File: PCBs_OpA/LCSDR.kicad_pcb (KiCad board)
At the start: 2 copper layers, 70 x 100 mm, 118 parts, among them CON2 AVR-ISP-6, J1 MIC, J10 SPK, J12 Conn_01x01, J13 Conn_01x01, J14 Conn_01x01, J15 Conn_01x01, J2 ANT, J3 USB_B, J4 CAL, J5 MEASURE, J6 I2C, J7 MEASURE, J8 Jack-DC, K1 TIANBO-HJR-4102-L, Q1 2N7002, Q2 2N7002, Q4 BS170, Q6 BS170, Q7 BF998, Q8 BS170, Q9 BC849, U1 74AC14, U2 Si5351, U3 FT232RL, U4 LM1117-5.0, U5 LM1117-3.3, U6 ATMEGA328P-AU, U7 NE5532, Y1 25Mhz, Y2 20Mhz

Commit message: operational amplifier Direct detection receiver
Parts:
- removed C23: 10nF, LCSDR:C_1206_0603
- removed L19: 1uH, Choke_Axial_ThroughHole:Choke_Horizontal_RM10mm
- added C21: 1nF, LCSDR:C_1206_0603, F.Cu at (146.6, 99.8)
- C45: value 330pF -> 360pF
- C47: value 220pF -> 360pF
- C49: value 330pF -> 1nF
- L10, L6, L8: footprint Choke_Axial_ThroughHole:Choke_Horizontal_RM20mm -> Choke_Toroid_ThroughHole:Choke_Toroid_6,5x13mm_Vertical
- L13: footprint Choke_Axial_ThroughHole:Choke_Horizontal_RM10mm -> Choke_Toroid_ThroughHole:Choke_Toroid_6,5x13mm_Vertical
- L15: footprint Resistors_THT:R_Axial_DIN0309_L9.0mm_D3.2mm_P2.54mm_Vertical -> Choke_Toroid_ThroughHole:Choke_Toroid_6,5x13mm_Vertical
- L17: value 680nH -> 1uH; footprint Choke_Axial_ThroughHole:Choke_Horizontal_RM10mm -> Choke_Toroid_ThroughHole:Choke_Toroid_6,5x13mm_Vertical
- moved C36 41.3 mm to (167.6, 66.8), turned to 90 degrees
- moved C9 33.0 mm to (139.2, 90.9), turned to 270 degrees
- moved L5 32.5 mm to (164.6, 121.9), turned to 180 degrees
- moved C34 32.3 mm to (156.2, 66.8)
- moved C27 31.9 mm to (164.8, 99.8), turned to 180 degrees
- moved Q8 30.7 mm to (167.9, 104.4)
- moved Q4 30.5 mm to (167.9, 112.0)
- moved Q6 30.4 mm to (167.9, 119.6)
- moved C25 29.2 mm to (161.0, 108.7), turned to 0 degrees
- moved C8 28.2 mm to (144.3, 95.2)
- moved R14 28.1 mm to (161.8, 122.4)
- moved K1 26.0 mm to (167.1, 84.1)
- moved D2 25.2 mm to (163.3, 91.7)
- moved L15 24.8 mm to (133.3, 108.0), turned to 0 degrees
- moved Q9 24.3 mm to (155.4, 91.9)
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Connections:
- C45 pad 1: RF_IN -> Net-(C21-Pad2)
- L13 pad 1: RF_IN -> Net-(C21-Pad2)
- Q7 pad 4: Net-(C23-Pad1) -> HPF
- R9 pad 1: Net-(C23-Pad1) -> HPF
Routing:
- net +12V: track 147.2 -> 32.5 mm, vias 4 -> 2
- net +5V: track 209.3 -> 108.5 mm, vias 6 -> 4
- net CLK0: track 57.5 -> 0.00 mm, vias 2 -> 0
- net Net-(C25-Pad1): track 49.0 -> 0.00 mm
- net Net-(C27-Pad1): track 43.7 -> 0.00 mm, vias 1 -> 0
- net Net-(C25-Pad2): track 40.2 -> 0.00 mm
- net RX_TX: track 30.1 -> 0.00 mm, vias 2 -> 0
- net Net-(C34-Pad1): track 28.6 -> 0.00 mm
- net LPF: track 27.5 -> 0.00 mm
- net +12VA: track 21.8 -> 0.00 mm
- net RF_IN: track 17.8 -> 0.00 mm, vias 1 -> 0
- net Net-(C30-Pad1): track 26.1 -> 12.0 mm
- net HPF: track 13.5 -> 0.63 mm, vias 1 -> 0
- net Net-(C32-Pad1): track 14.8 -> 2.80 mm
- net Net-(C45-Pad2): track 10.9 -> 0.00 mm
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
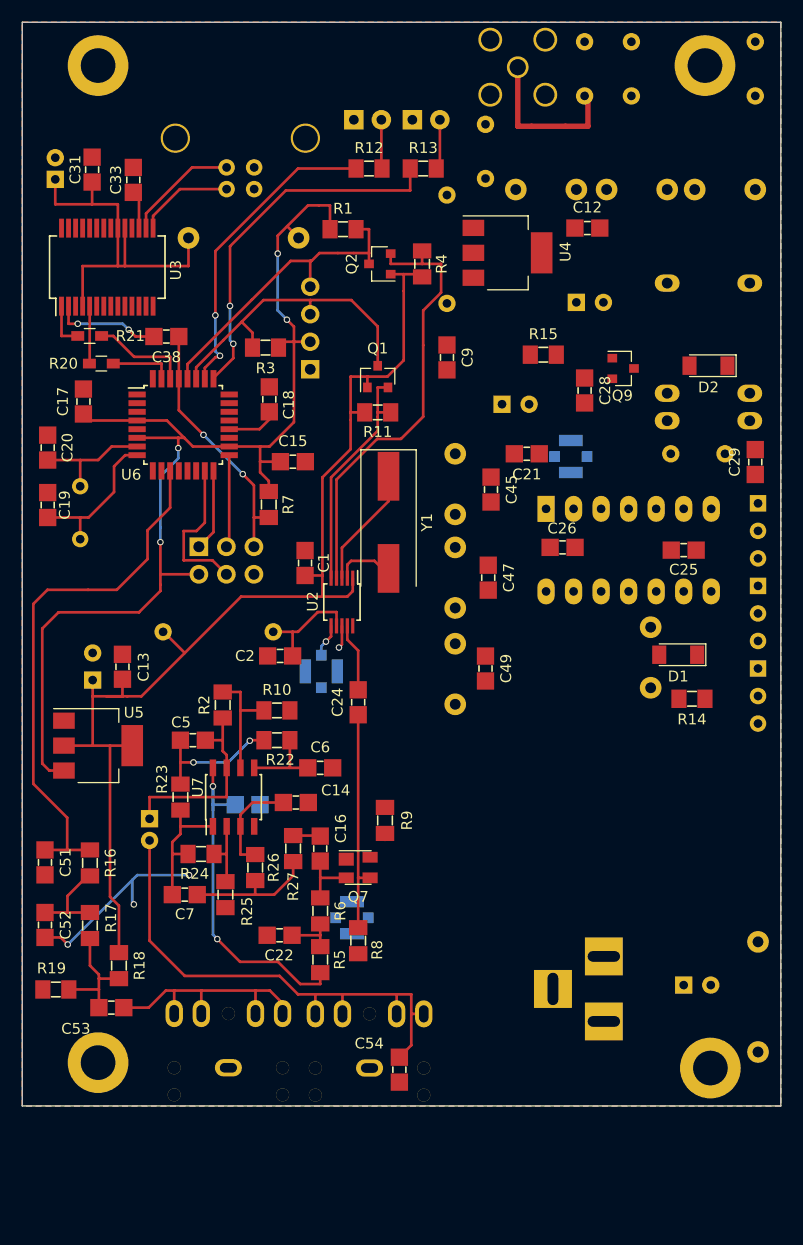
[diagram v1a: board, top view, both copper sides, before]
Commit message: add LPF/HPF RFSimm models
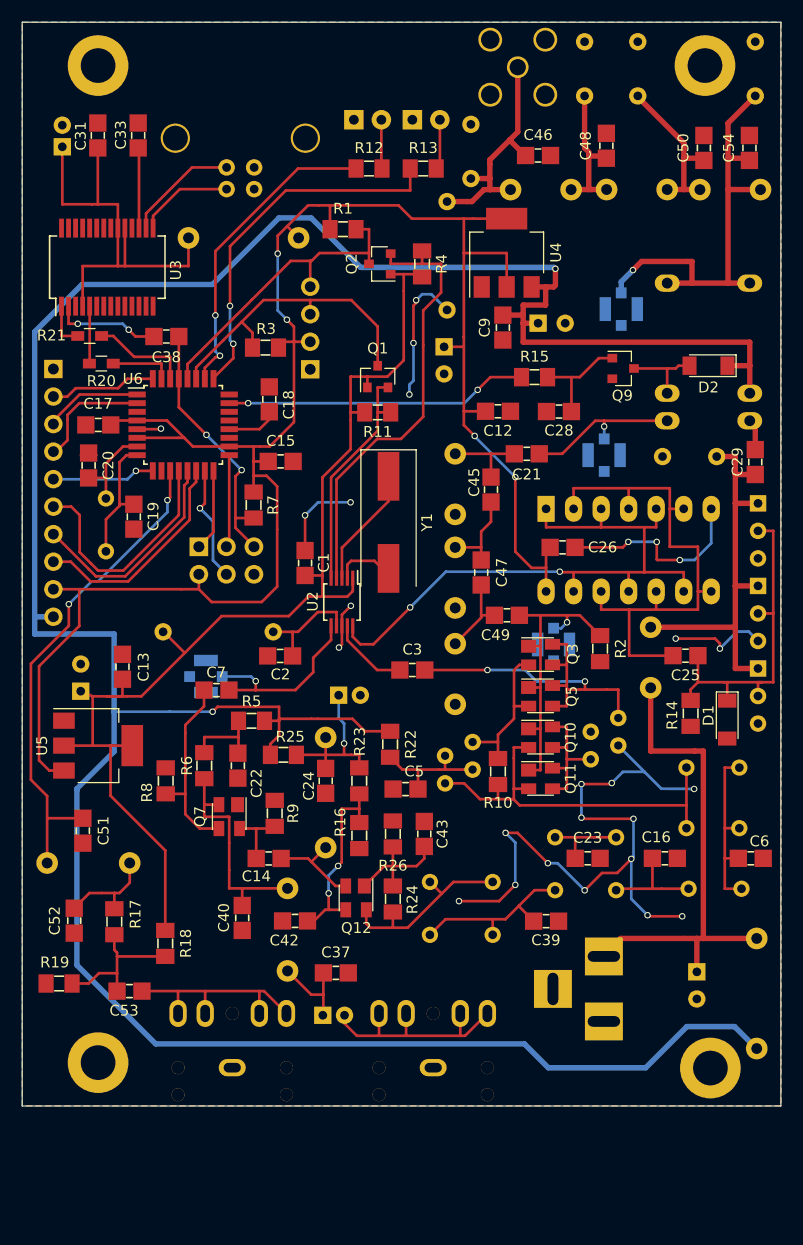
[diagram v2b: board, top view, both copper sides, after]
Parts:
- removed R27: 910, LCSDR:R_1206_0603
- removed U7: NE5532, Housings_SOIC:SOIC-8_3.9x4.9mm_Pitch1.27mm
- added C23: 56pF, LCSDR:C_1206_0603, F.Cu at (152.2, 137.2)
- added C37: 100nF, LCSDR:C_1206_0603, F.Cu at (128.9, 147.7)
- added C39: 56pF, LCSDR:C_1206_0603, F.Cu at (148.3, 142.9)
- added C40: 100nF, LCSDR:C_1206_0603, F.Cu at (120.3, 142.7)
- added C41: 10uF, Capacitors_THT:CP_Radial_D5.0mm_P2.00mm, B.Cu at (129.2, 122.1)
- added C42: 100nF, LCSDR:C_1206_0603, F.Cu at (125.2, 142.9)
- added C43: 100nF, LCSDR:C_1206_0603, F.Cu at (137.1, 134.9)
- added C46: 360pF, LCSDR:C_1206_0603, F.Cu at (147.6, 72.3)
- added C48: 750pF, LCSDR:C_1206_0603, F.Cu at (153.9, 71.4)
- added C50: 750pF, LCSDR:C_1206_0603, F.Cu at (162.9, 71.6)
- added J11: Conn_01x10, Pin_Headers:Pin_Header_Straight_1x10_Pitch2.54mm, B.Cu at (102.9, 92.0)
- added J9: MEASURE, LCSDR:U.FL_Molex_MCRF_73412-0110_Vertical, B.Cu at (155.3, 86.5)
- added L3: 100uH, Choke_Axial_ThroughHole:Choke_Horizontal_RM10mm, B.Cu at (128.0, 131.0)
- added L4: 100mH, Choke_Toroid_ThroughHole:Choke_Toroid_8x16mm_Vertical, B.Cu at (132.1, 147.5)
- added L7: 100mH, Choke_Toroid_ThroughHole:Choke_Toroid_8x16mm_Vertical, B.Cu at (102.3, 145.2)
- added Q10: BF998, TO_SOT_Packages_SMD:SOT-143, F.Cu at (147.8, 126.0)
- added Q11: BF998, TO_SOT_Packages_SMD:SOT-143, F.Cu at (147.8, 129.8)
- added Q12: BF998, TO_SOT_Packages_SMD:SOT-143, F.Cu at (130.8, 140.8)
- added Q3: BF998, TO_SOT_Packages_SMD:SOT-143, F.Cu at (147.8, 118.3)
- added Q5: BF998, TO_SOT_Packages_SMD:SOT-143, F.Cu at (147.8, 122.2)
- added T1: Transformer_1_4, LCSDR:TF14, B.Cu at (155.0, 124.2)
- added T2: Transformer_1_4, LCSDR:TF14, B.Cu at (141.6, 126.4)
- added Y3: Crystal, Crystals:Crystal_HC49-U_Vertical, B.Cu at (161.3, 134.4)
- added Y4: Crystal, Crystals:Crystal_HC49-U_Vertical, B.Cu at (161.3, 128.8)
- added Y5: Crystal, Crystals:Crystal_HC49-U_Vertical, B.Cu at (166.4, 140.0)
- added Y6: Crystal, Crystals:Crystal_HC49-U_Vertical, B.Cu at (154.8, 140.1)
- added Y7: Crystal, Crystals:Crystal_HC49-U_Vertical, B.Cu at (149.2, 135.2)
- added Y8: Crystal, Crystals:Crystal_HC49-U_Vertical, B.Cu at (137.6, 144.2)
- added Y9: Crystal, Crystals:Crystal_HC49-U_Vertical, B.Cu at (143.4, 144.2)
- C14, C7: value 27nF -> 10nF
- C16: value 1uF -> 56pF
- C24, C51, C52: value 10nF -> 100nF
- C3: value 100nF -> 10nF; moved to F.Cu
- C30, C36: value 270pF -> 360pF
- C32, C34: value 680pF -> 750pF
- C5: value 33nF -> 100nF
- C53: value 100nF -> 1uF
- C54: value 100nF -> 360pF
- C6: value 33nF -> 56pF
- L10, L6: value 1.32uH -> 1.22uH
- L8: value 1.72uH -> 1.42uH
- R10: value 910 -> 1.5K
- R16: value 10k -> 10K
- R2: value 2K -> 220
- R22: value 2.7K -> 100
- R23: value 1.2K -> 10K
- R24: value 2K -> 300
- R25: value 910 -> 100
- R26: value 5.1K -> 220
- moved C54 91.0 mm to (167.1, 71.6), turned to 90 degrees
- moved C6 40.6 mm to (167.2, 137.2)
- moved R2 35.2 mm to (153.3, 117.8)
- moved C16 31.8 mm to (159.3, 137.2), turned to 0 degrees
- moved J7 31.3 mm to (149.0, 117.4), turned to 0 degrees
- moved R16 25.0 mm to (131.1, 135.1)
- moved C4 24.2 mm to (127.7, 151.6), turned to 0 degrees
- moved R8 23.1 mm to (113.2, 130.0), turned to 90 degrees
- moved R5 22.9 mm to (121.2, 124.5), turned to 0 degrees
- moved R10 21.2 mm to (143.9, 129.1), turned to 90 degrees
- moved C5 20.1 mm to (135.4, 130.8), turned to 0 degrees
- moved C3 19.6 mm to (136.0, 119.8)
- moved C7 19.1 mm to (117.9, 121.6)
- moved C12 18.8 mm to (143.9, 95.9)
- moved R24 18.2 mm to (134.2, 140.9), turned to 90 degrees
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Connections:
- C14 pad 2: GND -> Net-(C14-Pad2)
- C16 pad 2: Net-(C16-Pad2) -> GND
- C24 pad 2: CLK1 -> GND
- C3 pad 1: +12V -> CLK1
- C3 pad 2: GND -> Net-(C3-Pad2)
- C4 pad 1: Net-(C4-Pad1) -> Net-(C37-Pad1)
- C5 pad 1: Net-(C4-Pad1) -> GND
- C51 pad 1: Net-(C51-Pad1) -> MIC
- C54 pad 1: Net-(C4-Pad2) -> LPF
- C7 pad 2: Net-(C7-Pad2) -> CLK2
- J4 pad 1: Net-(J4-Pad1) -> CLK2
- Q7 pad 2: Net-(C16-Pad2) -> Net-(C40-Pad1)
- Q7 pad 3: Net-(C24-Pad1) -> Net-(C7-Pad1)
- Q7 pad 4: HPF -> Net-(C14-Pad2)
- R10 pad 1: Net-(R10-Pad1) -> Net-(Q10-Pad2)
- R10 pad 2: GND -> Net-(Q3-Pad2)
- R16 pad 1: Net-(C51-Pad1) -> Net-(C42-Pad1)
- R16 pad 2: Net-(C52-Pad1) -> GND
- R2 pad 1: Net-(R10-Pad1) -> HPF
- R2 pad 2: Net-(C4-Pad1) -> GND
- R22 pad 1: Net-(C5-Pad2) -> +12V
- R22 pad 2: Net-(C6-Pad1) -> Net-(C5-Pad2)
- R23 pad 1: Net-(C7-Pad1) -> Net-(C24-Pad1)
- R23 pad 2: Net-(C5-Pad2) -> Net-(C42-Pad1)
- R24 pad 1: Net-(R24-Pad1) -> Net-(Q12-Pad4)
- R24 pad 2: Net-(C7-Pad1) -> Net-(C43-Pad1)
- R25 pad 1: Net-(R24-Pad1) -> +12V
- R25 pad 2: GND -> Net-(C24-Pad1)
- R26 pad 1: Net-(C7-Pad2) -> Net-(C43-Pad1)
- R26 pad 2: Net-(C14-Pad1) -> GND
- R6 pad 1: Net-(C16-Pad2) -> Net-(C40-Pad1)
- R8 pad 1: Net-(C24-Pad1) -> Net-(C7-Pad1)
- R9 pad 1: HPF -> Net-(C14-Pad2)
- U2 pad 6: Net-(J4-Pad1) -> CLK2
- U6 pad 1: (no net) -> IO_5
- U6 pad 11: Net-(C51-Pad1) -> MIC
- U6 pad 12: (no net) -> IO_8
- U6 pad 13: (no net) -> IO_9
- U6 pad 14: RX_TX -> IO_10
- U6 pad 2: (no net) -> IO_6
- U6 pad 23: (no net) -> RX_TX
- U6 pad 32: (no net) -> IO_4
- U6 pad 9: (no net) -> IO_7
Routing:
- net +12V: track 32.5 -> 267.5 mm
- net GND: track 20.6 -> 117.9 mm, vias 4 -> 26
- net +5V: track 108.5 -> 182.7 mm
- net CLK0: track 0.00 -> 59.3 mm, vias 0 -> 2
- net Net-(C25-Pad1): track 0.00 -> 49.6 mm
- net Net-(C51-Pad1): track 49.4 -> 0.00 mm
- net +12VA: track 0.00 -> 45.9 mm
- net MIC: track 0.00 -> 45.8 mm, vias 0 -> 2
- net LPF: track 0.00 -> 41.2 mm, vias 0 -> 1
- net Net-(Q10-Pad2): track 0.00 -> 37.6 mm
- net Net-(C27-Pad1): track 0.00 -> 37.2 mm
- net Net-(C3-Pad2): track 0.00 -> 34.3 mm, vias 0 -> 2
- net Net-(C25-Pad2): track 0.00 -> 31.5 mm
- net HPF: track 0.63 -> 29.1 mm, vias 0 -> 1
- net RX_TX: track 0.00 -> 28.0 mm, vias 0 -> 2
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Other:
- net class Default: trace_width 0.25 -> 0.5

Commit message: release gerber files
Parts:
- added J17: QER, Pin_Headers:Pin_Header_Straight_1x01_Pitch2.54mm, B.Cu at (142.2, 134.0)
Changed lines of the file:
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@@
 (kicad_pcb (version 4) (host pcbnew 4.0.7)
   (general
-    (links 326)
+    (links 327)
     (no_connects 0)
     (area 99.949999 59.949999 170.050001 160.050001)
@@
     (tracks 904)
     (zones 0)
-    (modules 144)
+    (modules 145)
     (nets 83)
   )
@@
     )
   )
+  (module Pin_Headers:Pin_Header_Straight_1x01_Pitch2.54mm (layer B.Cu)
+    (at 142.25 134)
+    (descr "Through hole straight pin header, 1x01, 2.54mm pitch, single row")
+    (tags "Through hole pin header THT 1x01 2.54mm single row")
+    (fp_text reference J17 (at -2.5 0.25 270) (layer B.SilkS)
+      (effects (font (size 1 1) (thickness 0.15)) (justify mirror))
+    )
+    (fp_text value QER (at 0 -2.33) (layer B.Fab)
+      (effects (font (size 1 1) (thickness 0.15)) (justify mirror))
+    )
+    (fp_line (start -0.635 1.27) (end 1.27 1.27) (layer B.Fab) (width 0.1))
+    (fp_line (start 1.27 1.27) (end 1.27 -1.27) (layer B.Fab) (width 0.1))
+    (fp_line (start 1.27 -1.27) (end -1.27 -1.27) (layer B.Fab) (width 0.1))
+    (fp_line (start -1.27 -1.27) (end -1.27 0.635) (layer B.Fab) (width 0.1))
+    (fp_line (start -1.27 0.635) (end -0.635 1.27) (layer B.Fab) (width 0.1))
+    (fp_line (start -1.33 -1.33) (end 1.33 -1.33) (layer B.SilkS) (width 0.12))
+    (fp_line (start -1.33 -1.27) (end -1.33 -1.33) (layer B.SilkS) (width 0.12))
+    (fp_line (start 1.33 -1.27) (end 1.33 -1.33) (layer B.SilkS) (width 0.12))
+    (fp_line (start -1.33 -1.27) (end 1.33 -1.27) (layer B.SilkS) (width 0.12))
+    (fp_line (start -1.33 0) (end -1.33 1.33) (layer B.SilkS) (width 0.12))
+    (fp_line (start -1.33 1.33) (end 0 1.33) (layer B.SilkS) (width 0.12))
+    (fp_line (start -1.8 1.8) (end -1.8 -1.8) (layer B.CrtYd) (width 0.05))
+    (fp_line (start -1.8 -1.8) (end 1.8 -1.8) (layer B.CrtYd) (width 0.05))
+    (fp_line (start 1.8 -1.8) (end 1.8 1.8) (layer B.CrtYd) (width 0.05))
+    (fp_line (start 1.8 1.8) (end -1.8 1.8) (layer B.CrtYd) (width 0.05))
+    (fp_text user %R (at 0 0 270) (layer B.Fab)
+      (effects (font (size 1 1) (thickness 0.15)) (justify mirror))
+    )
+    (pad 1 thru_hole rect (at 0 0) (size 1.7 1.7) (drill 1) (layers *.Cu *.Mask)
+      (net 1 GND))
+    (model ${KISYS3DMOD}/Pin_Headers.3dshapes/Pin_Header_Straight_1x01_Pitch2.54mm.wrl
+      (at (xyz 0 0 0))
+      (scale (xyz 1 1 1))
+      (rotate (xyz 0 0 0))
+    )
+  )
   (gr_line (start 170 60) (end 170 160) (angle 90) (layer Edge.Cuts) (width 0.1))
   (gr_line (start 100 60) (end 170 60) (angle 90) (layer Edge.Cuts) (width 0.1))
@@
   (segment (start 152.27506 75.439064) (end 152.525 75.438) (width 0.5) (layer F.Cu) (net 31) (status 10))
   (segment (start 152.525 75.438) (end 153.924 75.438) (width 0.5) (layer F.Cu) (net 31))
-  (segment (start 156.8 66.8) (end 156.8 66.9) (width 0.5) (layer F.Cu) (net 32) (status C00000))
-  (segment (start 156.8 66.9) (end 161.05 71.15) (width 0.5) (layer F.Cu) (net 32) (status 400000))
+  (segment (start 156.8 66.8) (end 156.8 66.9) (width 0.5) (layer F.Cu) (net 32))
+  (segment (start 156.8 66.9) (end 161.05 71.15) (width 0.5) (layer F.Cu) (net 32))
   (segment (start 161.05 71.15) (end 161.05 71.642) (width 0.5) (layer F.Cu) (net 32))
   (segment (start 162.9 72.55) (end 161.05 72.55) (width 0.5) (layer F.Cu) (net 32) (status 10))

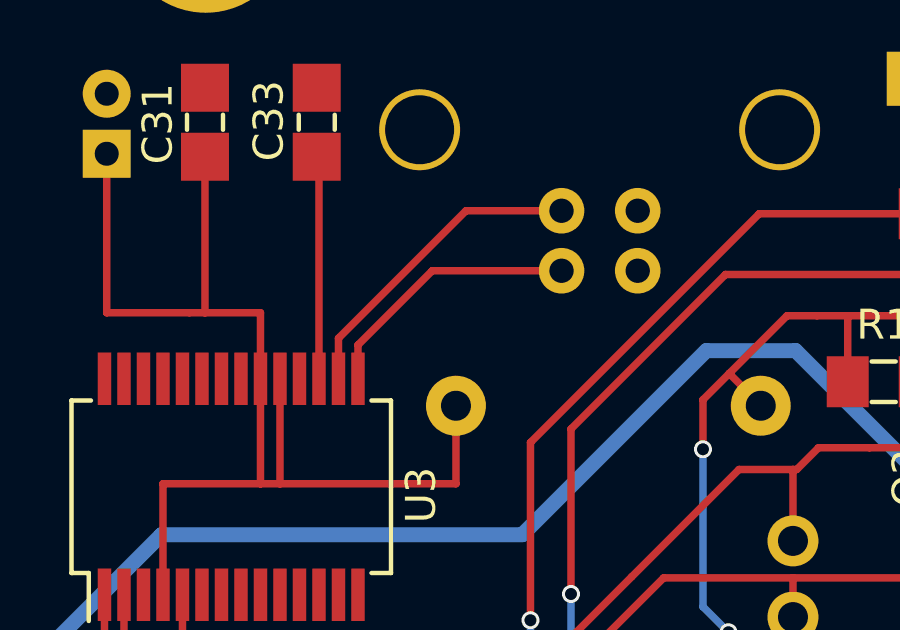
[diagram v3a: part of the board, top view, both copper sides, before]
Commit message: ADX988 CAT: add FE, FI commands
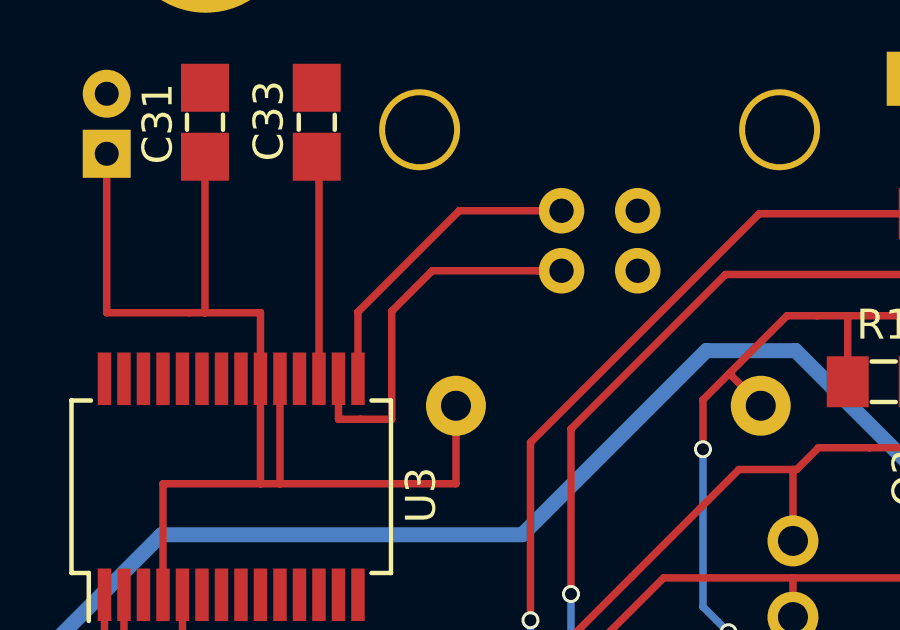
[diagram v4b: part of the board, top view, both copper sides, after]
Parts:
- C21, C49: value 1nF -> 680pF
- C45, C47: value 360pF -> 270pF
- L13, L17: value 1uH -> 900nH
- L15: value 680nH -> 800nH
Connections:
- J3 pad 1: (no net) -> Net-(J3-Pad1)
- U3 pad 10: (no net) -> Net-(U3-Pad10)
- U3 pad 11: (no net) -> Net-(U3-Pad11)
- U3 pad 12: (no net) -> Net-(U3-Pad12)
- U3 pad 13: (no net) -> Net-(U3-Pad13)
- U3 pad 14: (no net) -> Net-(U3-Pad14)
- U3 pad 15: Net-(J3-Pad2) -> Net-(J3-Pad3)
- U3 pad 16: Net-(J3-Pad3) -> Net-(J3-Pad2)
- U3 pad 22: (no net) -> Net-(U3-Pad22)
- U3 pad 23: (no net) -> Net-(U3-Pad23)
- U3 pad 27: (no net) -> Net-(U3-Pad27)
- U3 pad 28: (no net) -> Net-(U3-Pad28)
- U3 pad 3: (no net) -> Net-(U3-Pad3)
- U3 pad 6: (no net) -> Net-(U3-Pad6)
- U3 pad 9: (no net) -> Net-(U3-Pad9)
- U6 pad 19: (no net) -> Net-(U6-Pad19)
- U6 pad 22: (no net) -> Net-(U6-Pad22)
- U6 pad 24: (no net) -> IO_1
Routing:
- net Net-(J3-Pad2): track 8.94 -> 12.9 mm
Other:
- net class Default: trace_width 0.5 -> 0.25

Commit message: Arduino Nano PCB ADX988 DSP
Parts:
- removed C17, C18, C31, C33: 100nF, LCSDR:C_1206_0603
- removed C44: 10uF, Capacitors_THT:CP_Radial_D5.0mm_P2.00mm
- removed D3: LED, LEDs:LED_D3.0mm_Horizontal_O3.81mm_Z10.0mm
- removed J11: Conn_01x10, Pin_Headers:Pin_Header_Straight_1x10_Pitch2.54mm
- removed L12: 10uH, Choke_Axial_ThroughHole:Choke_Horizontal_RM10mm
- removed Q1, Q2: 2N7002, TO_SOT_Packages_SMD:SOT-23
- removed R1, R3: 10K, LCSDR:R_1206_0603
- removed R12: 1k, LCSDR:R_1206_0603
- removed U6: ATMEGA328P-AU, Housings_QFP:TQFP-32_7x7mm_Pitch0.8mm
- added Q13: MMBT3904, TO_SOT_Packages_SMD:SOT-23, F.Cu at (123.0, 81.2)
- added Q14: MMBT3906, TO_SOT_Packages_SMD:SOT-23, F.Cu at (111.3, 78.9)
- added R27: 10K, Resistors_SMD:R_0603_HandSoldering, F.Cu at (119.8, 80.2)
- added R28: 4.7k, Resistors_SMD:R_0603_HandSoldering, F.Cu at (118.3, 71.0)
- J3: value USB_B -> RJ45; footprint Connectors:USB_B -> Connectors:RJ45_8
- R20: value 1K -> 4.7k
- U3: value FT232RL -> ATtiny1614-SS; footprint Housings_SSOP:SSOP-28_5.3x10.2mm_Pitch0.65mm -> Housings_SOIC:SOIC-14_3.9x8.7mm_Pitch1.27mm
- moved C15 70.4 mm to (135.0, 170.1)
- moved C38 20.2 mm to (127.0, 74.2)
- moved R20 14.4 mm to (116.3, 80.2), turned to 0 degrees
- moved U3 11.4 mm to (116.2, 90.3), turned to 0 degrees
- moved R21 8.73 mm to (111.5, 82.0)
- moved J3 6.75 mm to (114.8, 74.2), turned to 0 degrees
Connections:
- C15 pad 1: +5V -> +3V3
- CON2 pad 1: Net-(CON2-Pad1) -> (no net)
- CON2 pad 3: Net-(CON2-Pad3) -> (no net)
- CON2 pad 4: Net-(CON2-Pad4) -> (no net)
- CON2 pad 5: RESET -> (no net)
- J3 pad 1: Net-(J3-Pad1) -> (no net)
- J3 pad 2: Net-(J3-Pad2) -> (no net)
- J3 pad 4: GND -> (no net)
- J6 pad 2: +5V -> +3V3
- R11 pad 2: Net-(Q1-Pad2) -> SDA
- R20 pad 1: TxD -> +3V3
- R20 pad 2: Net-(R20-Pad2) -> TxD
- R21 pad 2: Net-(R21-Pad2) -> Net-(Q14-Pad1)
- R4 pad 2: Net-(Q2-Pad2) -> SCL
- R7 pad 2: RESET -> (no net)
- U2 pad 4: Net-(Q2-Pad2) -> SCL
- U2 pad 5: Net-(Q1-Pad2) -> SDA
- U3 pad 1: Net-(R21-Pad2) -> +3V3
- U3 pad 10: Net-(U3-Pad10) -> RESET
- U3 pad 11: Net-(U3-Pad11) -> RxD
- U3 pad 12: Net-(U3-Pad12) -> TxD
- U3 pad 13: Net-(U3-Pad13) -> (no net)
- U3 pad 14: Net-(U3-Pad14) -> GND
- U3 pad 2: Net-(C38-Pad2) -> LED_RED
- U3 pad 3: Net-(U3-Pad3) -> RX_TX
- U3 pad 4: Net-(C31-Pad1) -> MIC
- U3 pad 5: Net-(R20-Pad2) -> GND
- U3 pad 6: Net-(U3-Pad6) -> Net-(C20-Pad1)
- U3 pad 7: GND -> Net-(C19-Pad1)
- U3 pad 8: (no net) -> SDA
- U3 pad 9: Net-(U3-Pad9) -> SCL
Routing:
- net +12V: track 267.5 -> 184.4 mm, vias 2 -> 1
- net +5V: track 182.7 -> 114.3 mm, vias 4 -> 2
- net Net-(Q2-Pad2): track 41.1 -> 0.00 mm
- net Net-(C31-Pad1): track 40.9 -> 0.00 mm
- net MIC: track 45.8 -> 7.43 mm, vias 2 -> 0
- net +3V3: track 108.1 -> 72.9 mm
- net LED_RED: track 33.9 -> 0.00 mm, vias 2 -> 0
- net (no net): track 0.00 -> 31.9 mm, vias 0 -> 1
- net SDA: track 29.1 -> 0.00 mm
- net LED_GREEN: track 28.8 -> 0.00 mm, vias 2 -> 0
- net RX_TX: track 28.0 -> 0.00 mm, vias 2 -> 0
- net RESET: track 24.4 -> 0.00 mm, vias 2 -> 0
- net IO_8: track 22.2 -> 0.00 mm
- net Net-(Q1-Pad2): track 21.5 -> 0.00 mm
- net IO_9: track 20.5 -> 0.00 mm
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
